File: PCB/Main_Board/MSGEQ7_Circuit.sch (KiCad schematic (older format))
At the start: 8 parts, among them U5 MSGEQ7

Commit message: Add IR circuit
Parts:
- renumbered U5 to U6
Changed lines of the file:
@@
 AR Path="/5FAF419F/5FA62242" Ref="RV?"  Part="1"
 AR Path="/5FAFFB20/5FA62242" Ref="RV1"  Part="1"
-F 0 "RV3" H 981 2096 50  0000 R CNN
+F 0 "RV1" H 981 2096 50  0000 R CNN
 F 1 "47k_POT_TRIM" H 981 2005 50  0000 R CNN
 F 2 "" H 1050 2050 50  0001 C CNN
@@
 AR Path="/5FAF419F/5FA62243" Ref="RV?"  Part="1"
 AR Path="/5FAFFB20/5FA62243" Ref="RV2"  Part="1"
-F 0 "RV4" H 1331 2396 50  0000 R CNN
+F 0 "RV2" H 1331 2396 50  0000 R CNN
 F 1 "47k_POT_TRIM" H 1331 2305 50  0000 R CNN
 F 2 "" H 1400 2350 50  0001 C CNN
@@
 AR Path="/5FAF419F/5FA537B5" Ref="C?"  Part="1"
 AR Path="/5FAFFB20/5FA537B5" Ref="C14"  Part="1"
-F 0 "C18" H 2042 2546 50  0000 L CNN
+F 0 "C14" H 2042 2546 50  0000 L CNN
 F 1 "33pF" H 2042 2455 50  0000 L CNN
 F 2 "" H 1950 2500 50  0001 C CNN
@@
 AR Path="/5FAF419F/5FA537B6" Ref="R?"  Part="1"
 AR Path="/5FAFFB20/5FA537B6" Ref="R9"  Part="1"
-F 0 "R10" H 1809 2396 50  0000 L CNN
+F 0 "R9" H 1809 2396 50  0000 L CNN
 F 1 "180k" H 1809 2305 50  0000 L CNN
 F 2 "" H 1750 2350 50  0001 C CNN
@@
 AR Path="/5FAF419F/5FA537B7" Ref="C?"  Part="1"
 AR Path="/5FAFFB20/5FA537B7" Ref="C13"  Part="1"
-F 0 "C17" H 1992 2096 50  0000 L CNN
+F 0 "C13" H 1992 2096 50  0000 L CNN
 F 1 "0.01uF" H 1992 2005 50  0000 L CNN
 F 2 "" H 1900 2050 50  0001 C CNN
@@
 AR Path="/5FAF419F/5FA30A38" Ref="C?"  Part="1"
 AR Path="/5FAFFB20/5FA30A38" Ref="C15"  Part="1"
-F 0 "C19" H 2892 1546 50  0000 L CNN
+F 0 "C15" H 2892 1546 50  0000 L CNN
 F 1 "0.1uF" H 2892 1455 50  0000 L CNN
 F 2 "" H 2800 1500 50  0001 C CNN
@@
 P 2550 2050
 AR Path="/5FA6223C" Ref="U?"  Part="1"
-AR Path="/5FA245CD/5FA6223C" Ref="U5"  Part="1"
+AR Path="/5FA245CD/5FA6223C" Ref="U6"  Part="1"
 AR Path="/5FA32A05/5FA6223C" Ref="U?"  Part="1"
 AR Path="/5FA51921/5FA6223C" Ref="U?"  Part="1"
 AR Path="/5FAD2BE2/5FA6223C" Ref="U?"  Part="1"
 AR Path="/5FAF419F/5FA6223C" Ref="U?"  Part="1"
-AR Path="/5FAFFB20/5FA6223C" Ref="U4"  Part="1"
+AR Path="/5FAFFB20/5FA6223C" Ref="U5"  Part="1"
 F 0 "U5" H 2550 2731 50  0000 C CNN
 F 1 "MSGEQ7" H 2550 2640 50  0000 C CNN
@@
 AR Path="/5FAF419F/5FA6223E" Ref="C?"  Part="1"
 AR Path="/5FAFFB20/5FA6223E" Ref="C16"  Part="1"
-F 0 "C20" H 3192 2546 50  0000 L CNN
+F 0 "C16" H 3192 2546 50  0000 L CNN
 F 1 "0.1uF" H 3192 2455 50  0000 L CNN
 F 2 "" H 3100 2500 50  0001 C CNN

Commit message: Further schematic work and footprint association
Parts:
- removed RV3, RV4: 47k_POT_TRIM, symbol Device:R_POT_TRIM
- added VR3, VR4: TC42X-2-503E, SamacSys:TC42X2503E, symbol SamacSys:TC42X-2-503E
- C17, C18, C19, C20: footprint (none) -> Capacitor_SMD:C_0603_1608Metric_Pad1.05x0.95mm_HandSolder
- R10: footprint (none) -> Resistor_SMD:R_0603_1608Metric_Pad1.05x0.95mm_HandSolder
- U6: footprint (none) -> Package_DIP:DIP-8_W7.62mm_Socket
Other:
- moved on the sheet: C13, C14, C15, C16, R9, U5

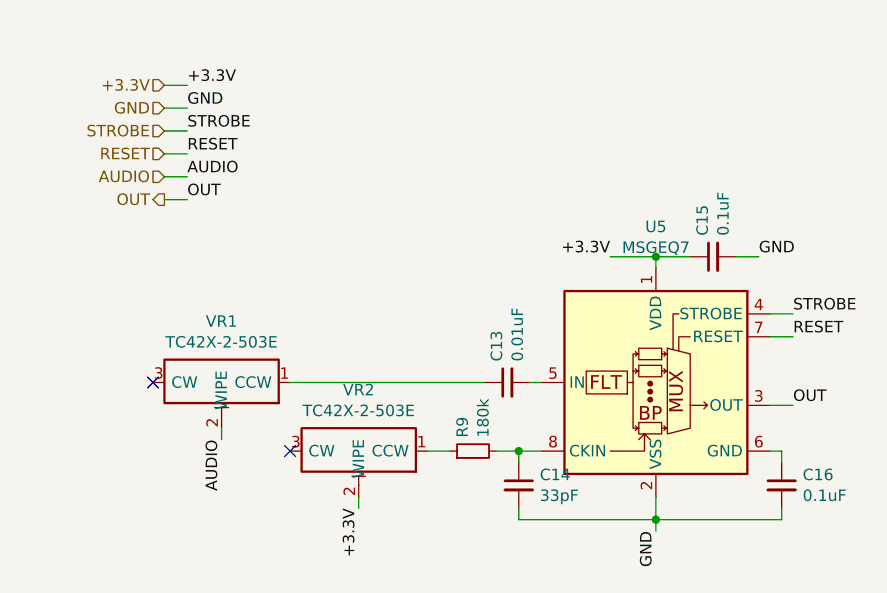
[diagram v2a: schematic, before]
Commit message: Further sourcing on mouser
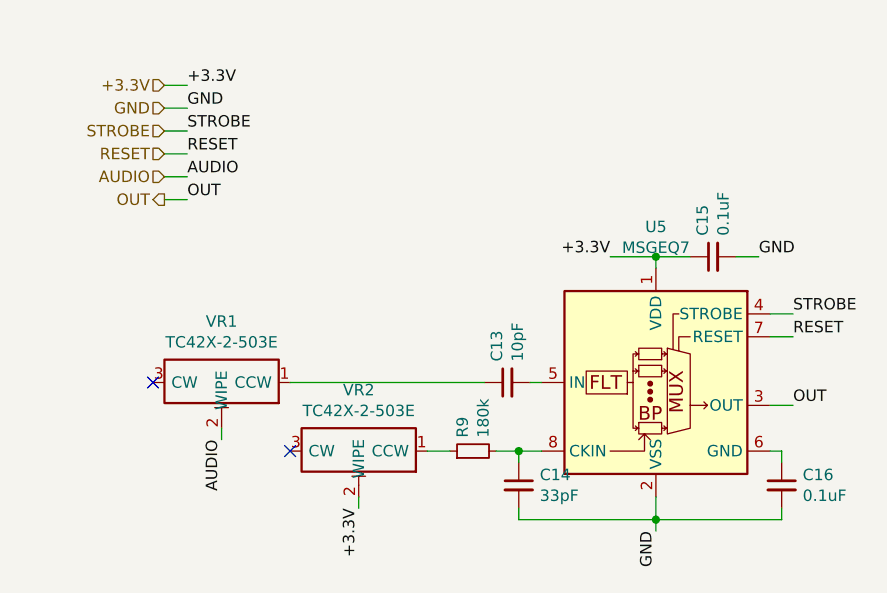
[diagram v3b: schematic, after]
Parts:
- C17: value 0.01uF -> 10pF
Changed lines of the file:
@@
 AR Path="/5FAFFB20/5FA537B7" Ref="C13"  Part="1"
 F 0 "C13" H 2692 2146 50  0000 L CNN
-F 1 "0.01uF" H 2692 2055 50  0000 L CNN
+F 1 "10pF" H 2692 2055 50  0000 L CNN
 F 2 "Capacitor_SMD:C_0603_1608Metric_Pad1.05x0.95mm_HandSolder" H 2600 2100 50  0001 C CNN
 F 3 "~" H 2600 2100 50  0001 C CNN

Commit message: PCB Layout work
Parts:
- C17: value 10pF -> 10nF
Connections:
- net at VR4.1 (CCW): no longer R10.1
- net at VR4.3 (CW): now also R10.1
- net at VR3.1 (CCW): no longer C17.1
- net at VR3.3 (CW): now also C17.1
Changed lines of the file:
@@
 $Descr A4 11693 8268
 encoding utf-8
-Sheet 3 4
+Sheet 4 4
 Title ""
 Date ""
@@
 AR Path="/5FAF419F/5FA6223E" Ref="C?"  Part="1"
 AR Path="/5FAFFB20/5FA6223E" Ref="C16"  Part="1"
-F 0 "C16" H 3892 2596 50  0000 L CNN
+F 0 "C20" H 3892 2596 50  0000 L CNN
 F 1 "0.1uF" H 3892 2505 50  0000 L CNN
 F 2 "Capacitor_SMD:C_0603_1608Metric_Pad1.05x0.95mm_HandSolder" H 3800 2550 50  0001 C CNN
@@
 AR Path="/5FAF419F/5FA6223C" Ref="U?"  Part="1"
 AR Path="/5FAFFB20/5FA6223C" Ref="U5"  Part="1"
-F 0 "U5" H 3250 2781 50  0000 C CNN
+F 0 "U6" H 3250 2781 50  0000 C CNN
 F 1 "MSGEQ7" H 3250 2690 50  0000 C CNN
 F 2 "Package_DIP:DIP-8_W7.62mm_Socket" H 3250 2100 50  0001 C CNN
@@
 AR Path="/5FAF419F/5FA30A38" Ref="C?"  Part="1"
 AR Path="/5FAFFB20/5FA30A38" Ref="C15"  Part="1"
-F 0 "C15" H 3592 1596 50  0000 L CNN
+F 0 "C19" H 3592 1596 50  0000 L CNN
 F 1 "0.1uF" H 3592 1505 50  0000 L CNN
 F 2 "Capacitor_SMD:C_0603_1608Metric_Pad1.05x0.95mm_HandSolder" H 3500 1550 50  0001 C CNN
@@
 AR Path="/5FAF419F/5FA537B7" Ref="C?"  Part="1"
 AR Path="/5FAFFB20/5FA537B7" Ref="C13"  Part="1"
-F 0 "C13" H 2692 2146 50  0000 L CNN
-F 1 "10pF" H 2692 2055 50  0000 L CNN
+F 0 "C17" H 2692 2146 50  0000 L CNN
+F 1 "10nF" H 2692 2055 50  0000 L CNN
 F 2 "Capacitor_SMD:C_0603_1608Metric_Pad1.05x0.95mm_HandSolder" H 2600 2100 50  0001 C CNN
 F 3 "~" H 2600 2100 50  0001 C CNN
@@
 AR Path="/5FAF419F/5FA537B6" Ref="R?"  Part="1"
 AR Path="/5FAFFB20/5FA537B6" Ref="R9"  Part="1"
-F 0 "R9" H 2509 2446 50  0000 L CNN
+F 0 "R10" H 2509 2446 50  0000 L CNN
 F 1 "180k" H 2509 2355 50  0000 L CNN
 F 2 "Resistor_SMD:R_0603_1608Metric_Pad1.05x0.95mm_HandSolder" H 2450 2400 50  0001 C CNN
@@
 AR Path="/5FAF419F/5FA537B5" Ref="C?"  Part="1"
 AR Path="/5FAFFB20/5FA537B5" Ref="C14"  Part="1"
-F 0 "C14" H 2742 2596 50  0000 L CNN
+F 0 "C18" H 2742 2596 50  0000 L CNN
 F 1 "33pF" H 2742 2505 50  0000 L CNN
 F 2 "Capacitor_SMD:C_0603_1608Metric_Pad1.05x0.95mm_HandSolder" H 2650 2550 50  0001 C CNN
@@
 AR Path="/5FA245CD/5F57BA41" Ref="VR4"  Part="1"
 AR Path="/5FAFFB20/5F57BA41" Ref="VR2"  Part="1"
-F 0 "VR2" V 1683 2400 50  0000 C CNN
+F 0 "VR4" V 1683 2400 50  0000 C CNN
 F 1 "TC42X-2-503E" V 1774 2400 50  0000 C CNN
 F 2 "SamacSys:TC42X2503E" H 2900 2500 50  0001 L CNN
@@
 F 9 "TC42X-2-503E" H 2900 1800 50  0001 L CNN "Manufacturer_Part_Number"
 	1    1950 2400
-	0    1    1    0
-$EndComp
-NoConn ~ 1650 2400
+	0    -1   1    0
+$EndComp
 $Comp
 L SamacSys:TC42X-2-503E VR3
@@
 AR Path="/5FA245CD/5F5A2DFD" Ref="VR3"  Part="1"
 AR Path="/5FAFFB20/5F5A2DFD" Ref="VR1"  Part="1"
-F 0 "VR1" V 1083 2100 50  0000 C CNN
+F 0 "VR3" V 1083 2100 50  0000 C CNN
 F 1 "TC42X-2-503E" V 1174 2100 50  0000 C CNN
 F 2 "SamacSys:TC42X2503E" H 2300 2200 50  0001 L CNN
@@
 F 9 "TC42X-2-503E" H 2300 1500 50  0001 L CNN "Manufacturer_Part_Number"
 	1    1350 2100
-	0    1    1    0
-$EndComp
-NoConn ~ 1050 2100
+	0    -1   1    0
+$EndComp
 Wire Wire Line
 	1650 2100 2500 2100
@@
 Wire Wire Line
 	1350 2350 1350 2300
+NoConn ~ 1650 2400
+NoConn ~ 1050 2100
 $EndSCHEMATC
